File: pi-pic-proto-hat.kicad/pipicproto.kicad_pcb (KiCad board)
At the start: 2 copper layers, 65 x 56 mm, 33 parts, among them J1 Conn_01x02_Male, J10 Conn_01x13_Male, J2 Conn_01x02_Male, J22 Conn_01x13_Male, J3 Conn_01x02_Male, J4 Conn_01x02_Male, J5 Conn_01x02_Male, J6 Barrel_Jack_Switch, J7 Conn_01x20_Male, J8 Conn_01x06_Male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

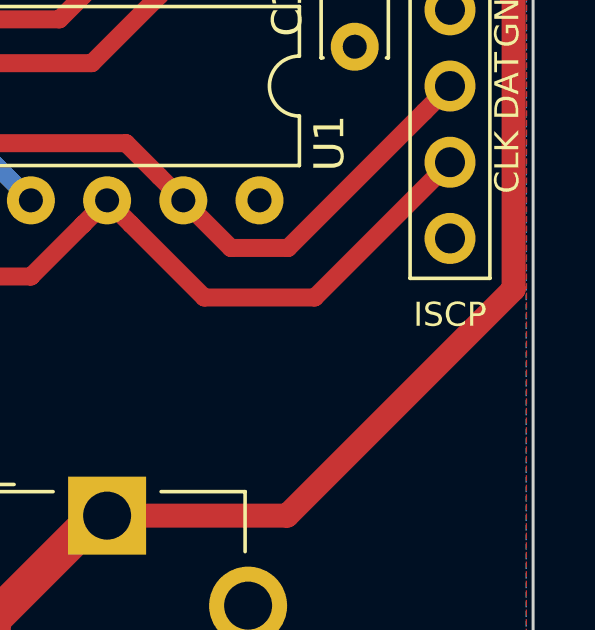
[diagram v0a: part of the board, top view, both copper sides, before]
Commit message: fix: changed label ISCP to ICSP
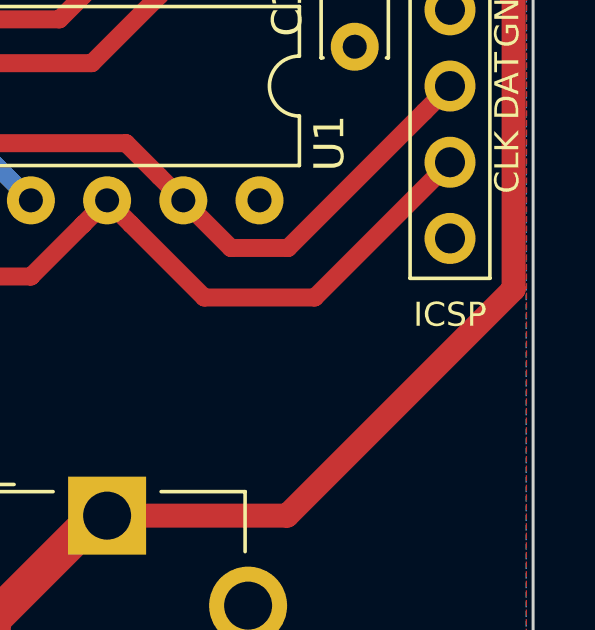
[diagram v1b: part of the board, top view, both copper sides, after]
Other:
- board text added: "ICSP"
- board text removed: "ISCP"
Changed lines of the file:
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@@
     (effects (font (size 1 1) (thickness 0.15)))
   )
-  (gr_text ISCP (at 262.23 129.68) (layer F.SilkS)
+  (gr_text ICSP (at 262.23 129.68) (layer F.SilkS)
     (effects (font (size 0.8 0.8) (thickness 0.1)))
   )

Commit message: V2.01: removed J4/J5/prototyping area
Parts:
- removed J4, J5: Conn_01x02_Male, Connector_PinHeader_2.54mm:PinHeader_1x02_P2.54mm_Vertical
- removed REF** (x2): Lora_3x5, myfootprint:Lora_3x5
- removed REF** (x4): Lora_5x5, myfootprint:Lora_5x5
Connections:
- J9 pad 6: /IO5 -> Net-(J9-Pad6)
- R2 pad 2: Net-(J4-Pad2) -> Net-(R2-Pad2)
- U1 pad 2: /IO5 -> Net-(R2-Pad2)
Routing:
- net Net-(R2-Pad2): track 0.00 -> 31.8 mm
- net /IO5: track 18.9 -> 0.00 mm
- net Net-(J4-Pad2): track 8.11 -> 0.00 mm
- net Net-(J4-Pad1): track 6.35 -> 0.00 mm

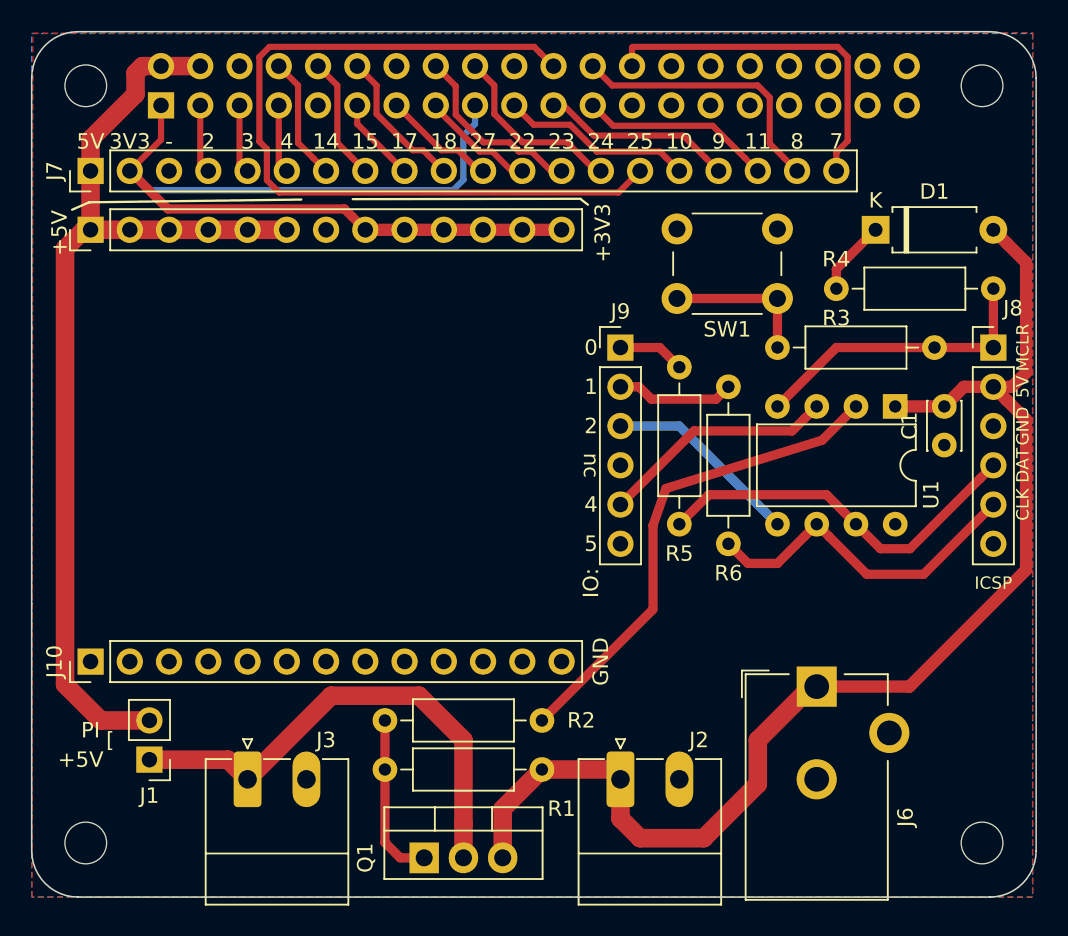
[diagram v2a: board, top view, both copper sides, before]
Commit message: V2.02: connect GP0/GP1 directly to the Pi (add voltage-divider for GP1)
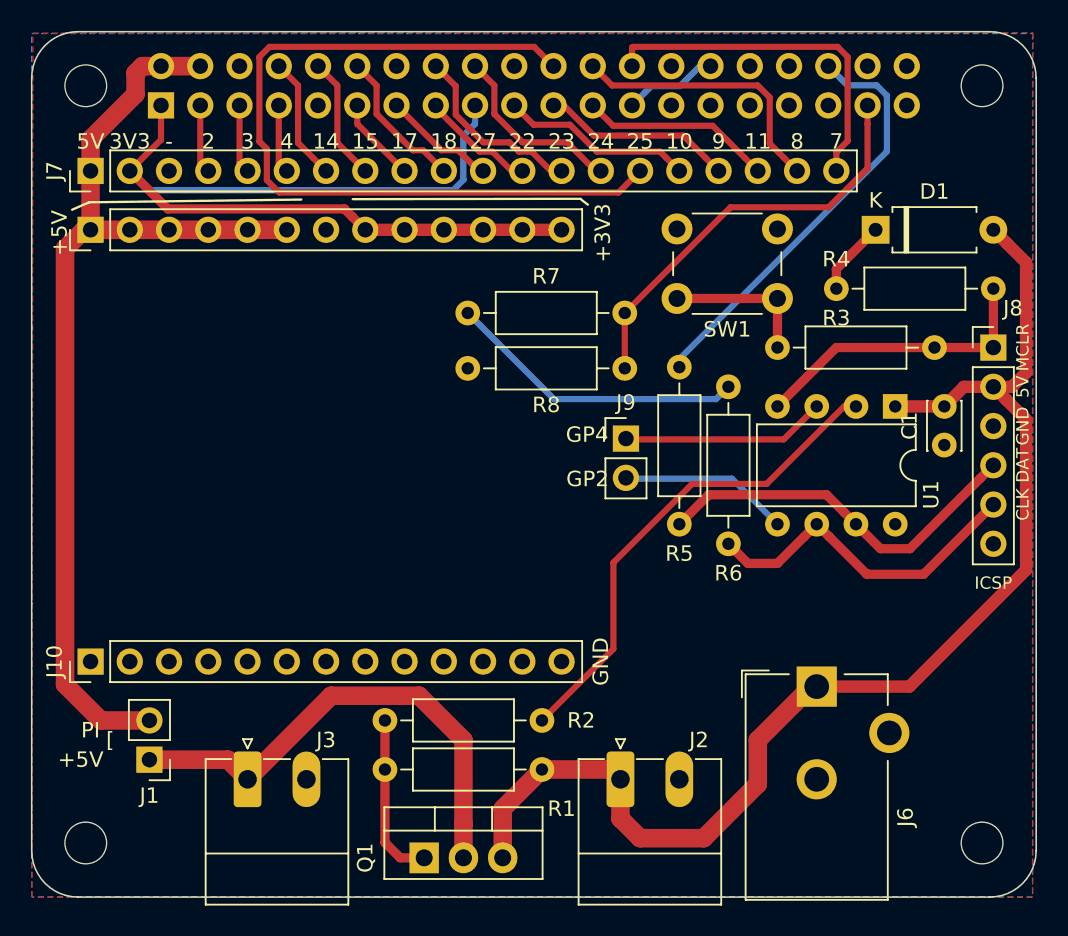
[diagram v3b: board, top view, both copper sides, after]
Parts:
- added R7: 6.2k, Resistor_THT:R_Axial_DIN0207_L6.3mm_D2.5mm_P10.16mm_Horizontal, F.Cu at (228.2, 112.2)
- added R8: 12k, Resistor_THT:R_Axial_DIN0207_L6.3mm_D2.5mm_P10.16mm_Horizontal, F.Cu at (238.4, 115.8)
- J9: value Conn_01x06_Male -> Conn_01x02_Male; footprint Connector_PinHeader_2.54mm:PinHeader_1x06_P2.54mm_Vertical -> Connector_PinHeader_2.54mm:PinHeader_1x02_P2.54mm_Vertical
- moved J9 5.90 mm to (238.5, 120.3)
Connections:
- net /GPIO7(SPI1_CE_N) renamed /GPIO7(SPI0_CE_1)
- net /GPIO8(SPI0_CE_N) renamed /GPIO8(SPI0_CE_0)
- J9 pad 1: /IO0 -> Net-(J9-Pad1)
- J9 pad 2: /IO1 -> Net-(J9-Pad2)
- R5 pad 2: /IO0 -> /GPIO16
- R6 pad 2: /IO1 -> Net-(R6-Pad2)
- U1 pad 3: /IO4 -> Net-(J9-Pad1)
- U1 pad 5: /IO2 -> Net-(J9-Pad2)
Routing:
- net /GPIO16: track 0.00 -> 27.7 mm
- net /GPIO26: track 0.00 -> 27.2 mm
- net Net-(R6-Pad2): track 0.00 -> 19.5 mm
- net /IO4: track 15.3 -> 0.00 mm
- net Net-(J9-Pad1): track 0.00 -> 12.8 mm
- net /IO2: track 12.8 -> 0.00 mm
- net Net-(J9-Pad2): track 0.00 -> 10.6 mm
- net /IO1: track 7.65 -> 0.00 mm
- net GND: track 0.00 -> 6.13 mm
- net /IO0: track 4.34 -> 0.00 mm
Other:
- net class Default: trace_width 0.2 -> 0.4
- board text added: "GP2"
- board text added: "GP4"
- board text removed: "0"
- board text removed: "1"
- board text removed: "5"
- board text removed: "IO:"
- board text removed: "nc"

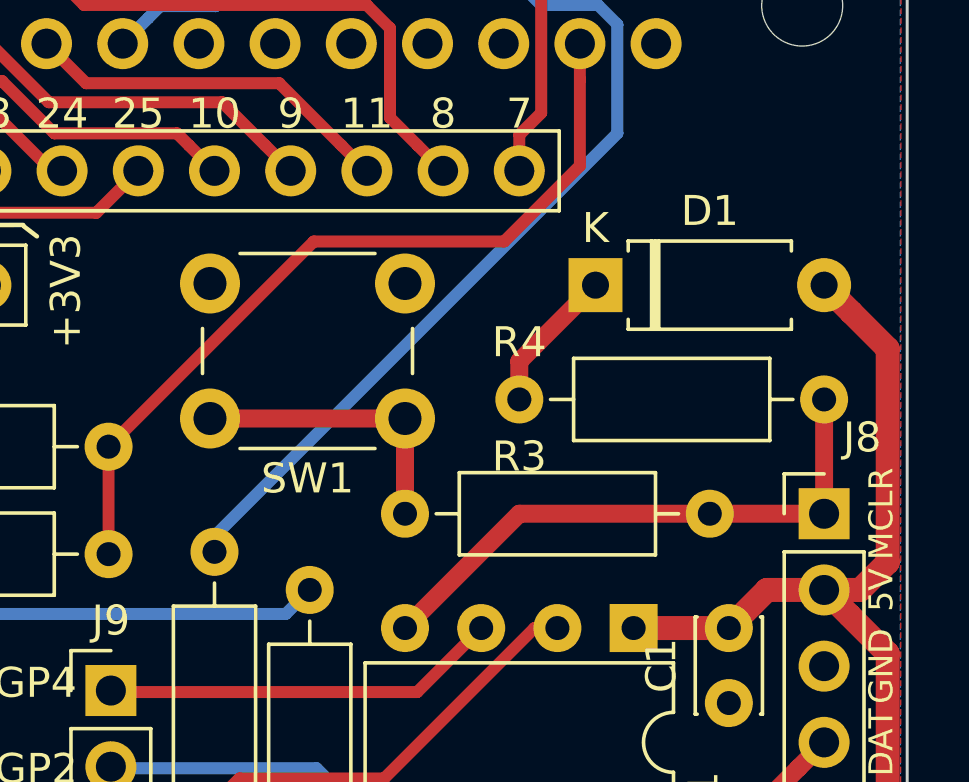
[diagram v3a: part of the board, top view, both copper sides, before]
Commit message: V2.03: removed reset-button, pullup, bat85
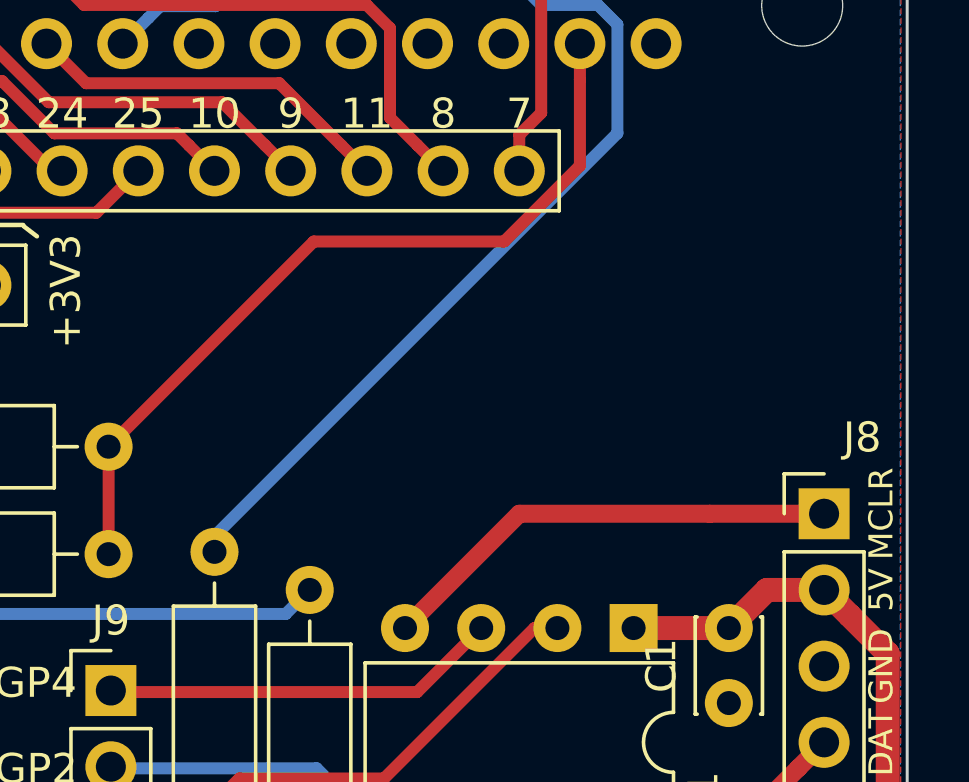
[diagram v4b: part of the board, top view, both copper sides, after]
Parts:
- removed D1: D_Schottky, Diode_THT:D_A-405_P7.62mm_Horizontal
- removed R3: 1k, Resistor_THT:R_Axial_DIN0207_L6.3mm_D2.5mm_P10.16mm_Horizontal
- removed R4: 22k, Resistor_THT:R_Axial_DIN0207_L6.3mm_D2.5mm_P10.16mm_Horizontal
- removed SW1: SW_Push, Button_Switch_THT:SW_PUSH_6mm_H9.5mm
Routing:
- net +5VP: track 82.5 -> 69.9 mm
- net Net-(R3-Pad2): track 9.67 -> 0.00 mm
- net Net-(D1-Pad1): track 4.86 -> 0.00 mm
- net /MCLR: track 19.4 -> 15.5 mm

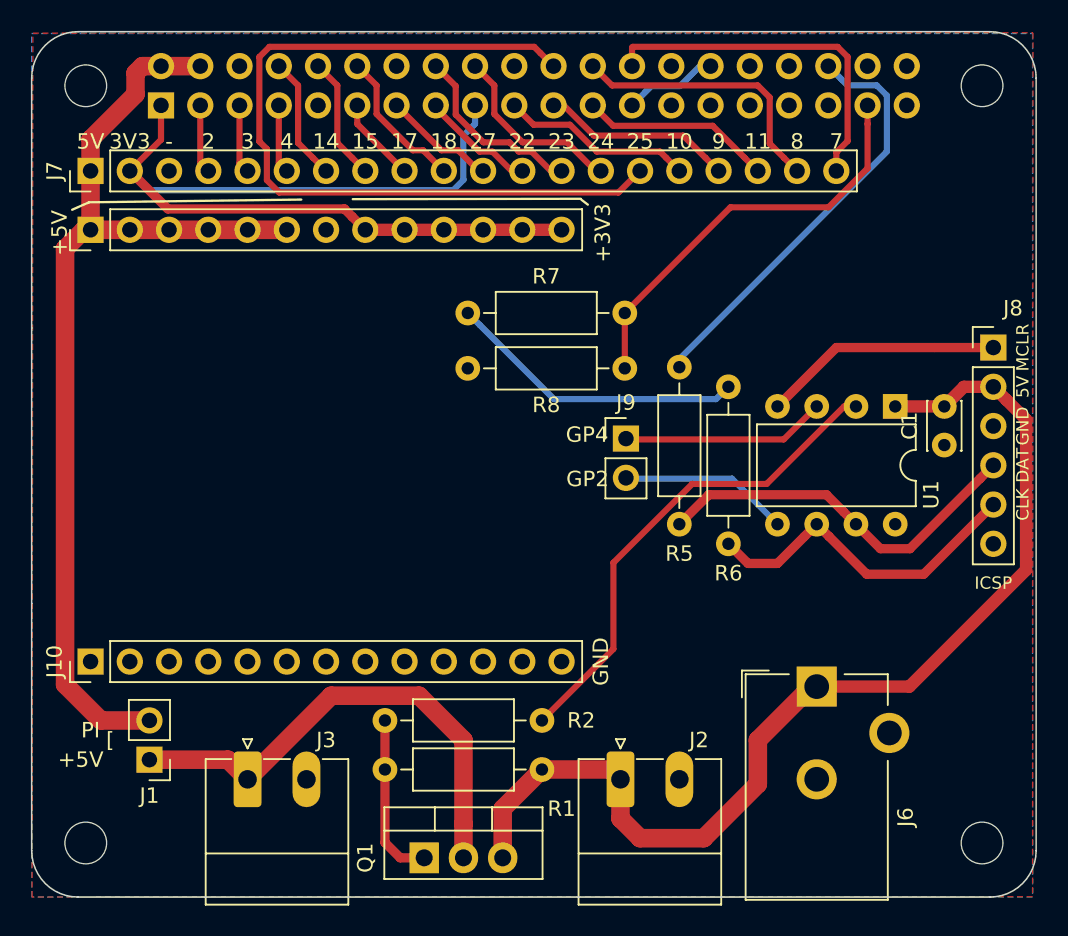
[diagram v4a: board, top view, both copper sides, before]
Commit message: moved voltage-divider to free area above PIC
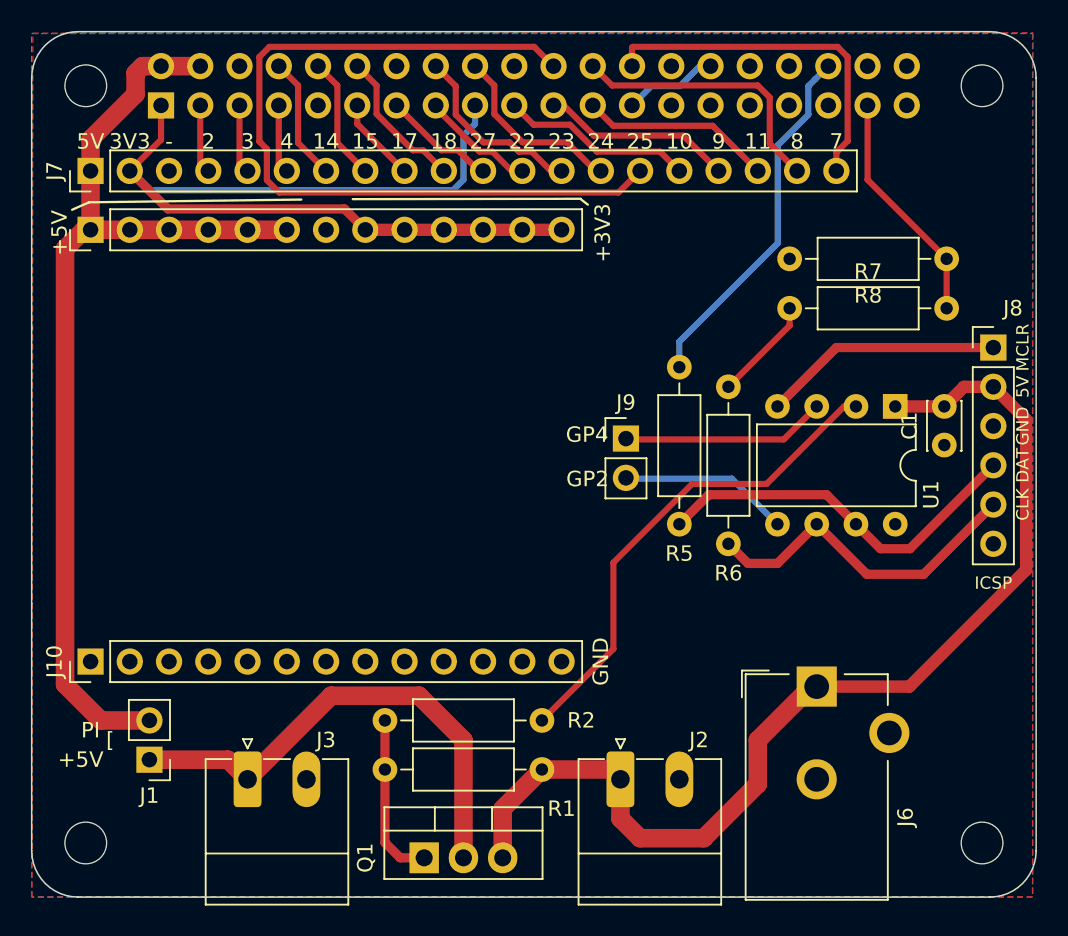
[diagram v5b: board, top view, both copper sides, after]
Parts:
- moved R8 22.0 mm to (259.2, 108.7)
- moved R7 20.8 mm to (249.0, 111.9)
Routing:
- net Net-(R6-Pad2): track 19.5 -> 6.72 mm
- net /GPIO26: track 27.2 -> 15.2 mm
- net /GPIO16: track 27.7 -> 23.5 mm

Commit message: V2.04: place jumper J1 between J6 (barrel-jack) and ICSP-connector
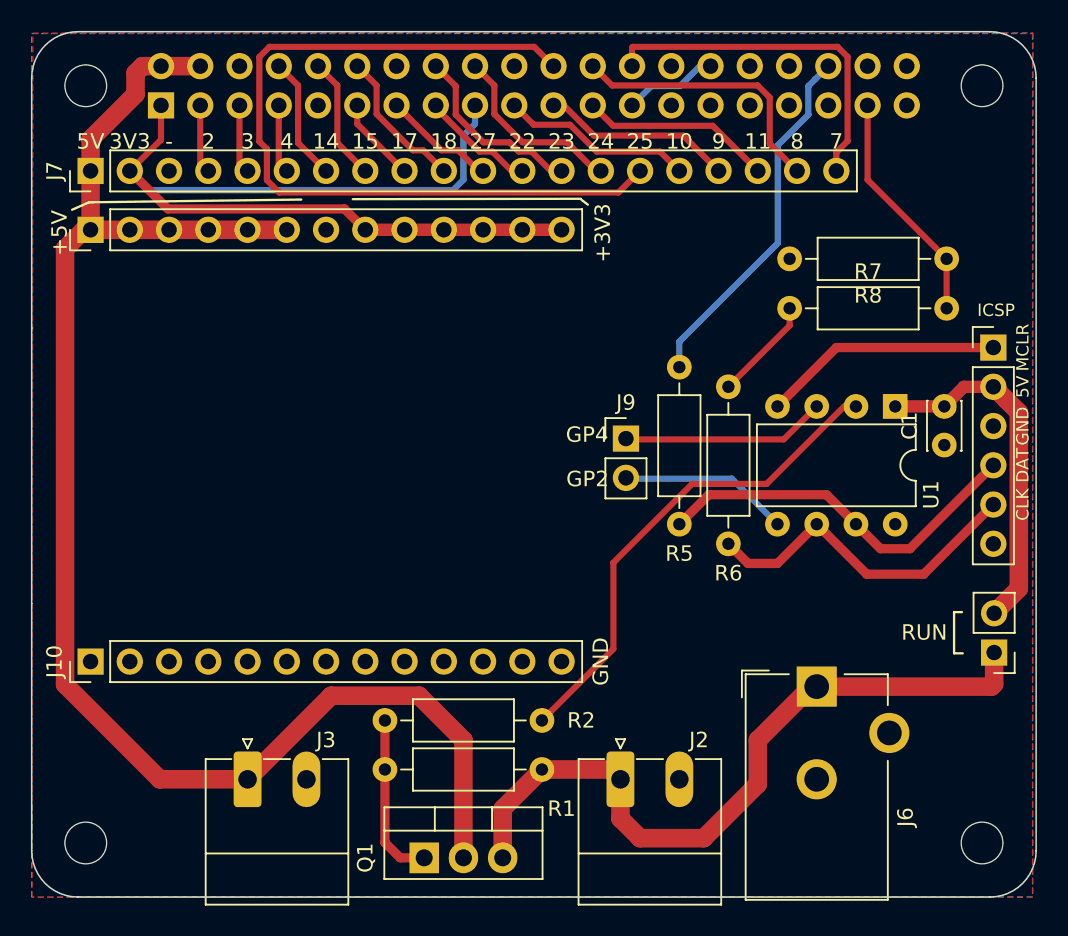
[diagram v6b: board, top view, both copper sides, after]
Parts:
- J1: value Conn_01x02_Male -> RUN/~PGM~
- moved J1 55.1 mm to (262.3, 134.2)
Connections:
- J1 pad 1: Net-(J1-Pad1) -> +5P
- J1 pad 2: +5V -> +5VP
- J2 pad 1: +5VP -> +5P
- J3 pad 1: Net-(J1-Pad1) -> +5V
- J6 pad 1: +5VP -> +5P
- Q1 pad 2: Net-(J1-Pad1) -> +5V
- Q1 pad 3: +5VP -> +5P
- R1 pad 1: +5VP -> +5P
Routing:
- net +5P: track 0.00 -> 47.2 mm
- net +5VP: track 69.9 -> 22.9 mm
- net +5V: track 65.2 -> 98.2 mm
- net Net-(J1-Pad1): track 31.9 -> 0.00 mm
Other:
- net class Power: trace_width 0.5 -> 1.2
- board text added: "RUN"
- board text removed: "PI"
- board text removed: "["
